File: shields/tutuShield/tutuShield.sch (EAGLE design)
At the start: 23 parts, among them IC1 IC_MSGEQ7-SOIC8, Q4 2N3904

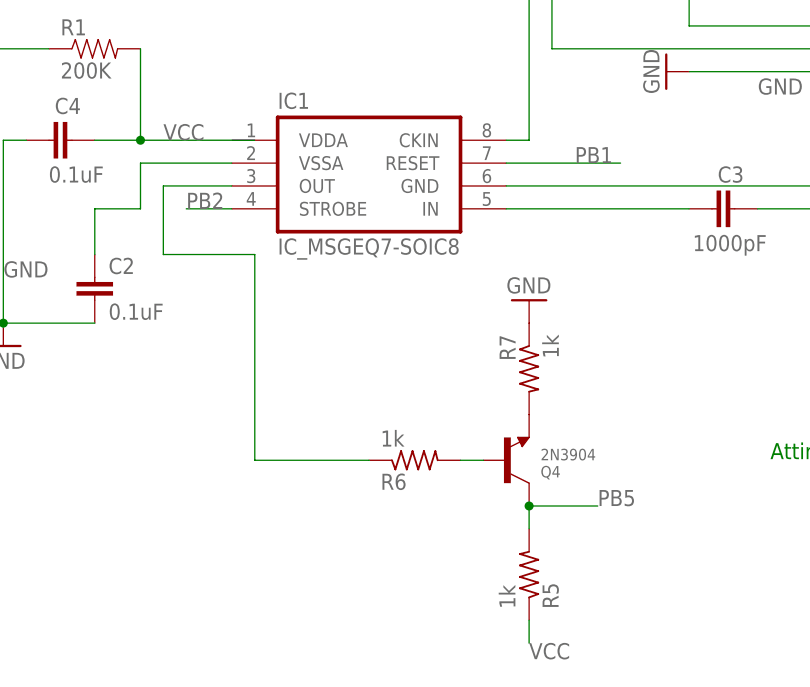
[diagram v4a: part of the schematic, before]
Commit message: a version without the PB5 trick
it might be a bit simpler but i think its worth it to stick to
4af68e7c457e82ac5364ccc3b228164f2045e11b
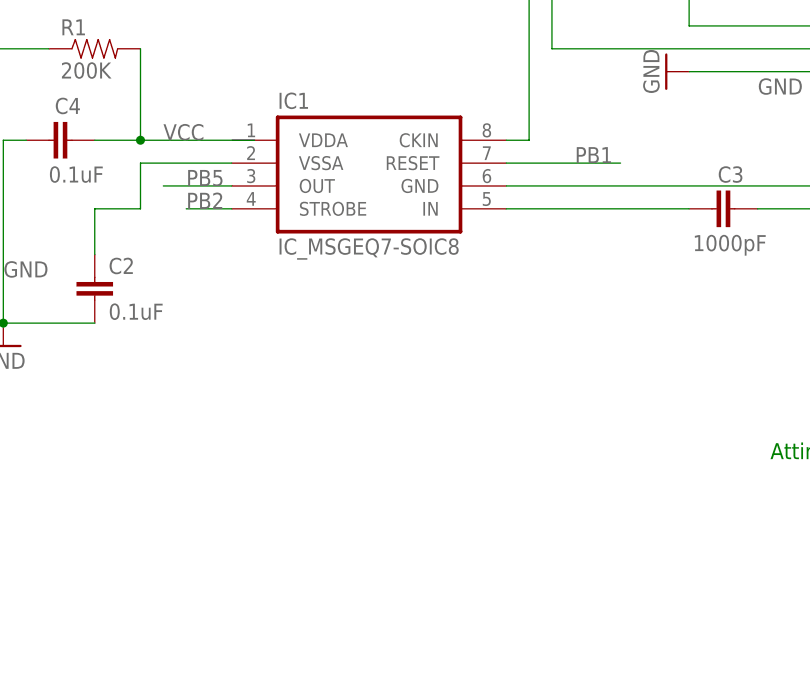
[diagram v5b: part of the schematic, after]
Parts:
- removed Q4: 2N3904, microbuilder:TRANSISTOR_NPNWAVE
- removed R5, R6, R7: 1k, adafruit:R-US_R0805
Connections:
- removed net N$14: Q4.B, R6.2
- removed net N$8: Q4.E, R7.2
- net GND: no longer R7.1
- net PB1: no longer IC1.OUT, R6.1
- net PB5: now also IC1.OUT; no longer Q4.C, R5.2
- net VCC: no longer R5.1
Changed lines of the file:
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@@
 <part name="JP2" library="ATtami" deviceset="HEADER-1X4" device="ROUND"/>
 <part name="GND3" library="SparkFun" deviceset="GND" device=""/>
-<part name="R5" library="adafruit" deviceset="R-US_" device="R0805" value="1k"/>
-<part name="Q4" library="microbuilder" deviceset="TRANSISTOR_NPN" device="WAVE" value="2N3904"/>
-<part name="R6" library="adafruit" deviceset="R-US_" device="R0805" value="1k"/>
-<part name="R7" library="adafruit" deviceset="R-US_" device="R0805" value="1k"/>
-<part name="GND4" library="SparkFun" deviceset="GND" device=""/>
 </parts>
 <sheets>
@@
 <instance part="JP2" gate="A" x="180.34" y="104.14"/>
 <instance part="GND3" gate="1" x="149.86" y="96.52" rot="R270"/>
-<instance part="R5" gate="G$1" x="134.62" y="40.64" rot="MR90"/>
-<instance part="Q4" gate="G$1" x="134.62" y="53.34" rot="MR180"/>
-<instance part="R6" gate="G$1" x="121.92" y="53.34" rot="MR180"/>
-<instance part="R7" gate="G$1" x="134.62" y="63.5" rot="MR270"/>
-<instance part="GND4" gate="1" x="134.62" y="71.12" rot="MR180"/>
 </instances>
 <busses>
@@
 <pinref part="GND3" gate="1" pin="GND"/>
 </segment>
-<segment>
-<pinref part="R7" gate="G$1" pin="1"/>
-<pinref part="GND4" gate="1" pin="GND"/>
-</segment>
 </net>
 <net name="VCC" class="0">
@@
 </segment>
 <segment>
-<pinref part="R5" gate="G$1" pin="1"/>
-<wire x1="134.62" y1="35.56" x2="134.62" y2="33.02" width="0.1524" layer="91"/>
-<label x="134.62" y="33.02" size="1.778" layer="95" rot="MR180"/>
-</segment>
-<segment>
 <pinref part="C3" gate="G$1" pin="2"/>
 <pinref part="JP1" gate="G$1" pin="2"/>
@@
 </segment>
 <segment>
-<pinref part="IC1" gate="IC" pin="OUT"/>
-<wire x1="101.6" y1="83.82" x2="93.98" y2="83.82" width="0.1524" layer="91"/>
-<wire x1="93.98" y1="83.82" x2="93.98" y2="76.2" width="0.1524" layer="91"/>
-<wire x1="93.98" y1="76.2" x2="104.14" y2="76.2" width="0.1524" layer="91"/>
-<wire x1="104.14" y1="76.2" x2="104.14" y2="53.34" width="0.1524" layer="91"/>
-<pinref part="R6" gate="G$1" pin="1"/>
-<wire x1="104.14" y1="53.34" x2="116.84" y2="53.34" width="0.1524" layer="91"/>
-</segment>
-<segment>
 <pinref part="IC1" gate="IC" pin="RESET"/>
 <wire x1="132.08" y1="86.36" x2="144.78" y2="86.36" width="0.1524" layer="91"/>
@@
 </segment>
 <segment>
-<pinref part="R5" gate="G$1" pin="2"/>
-<pinref part="Q4" gate="G$1" pin="C"/>
-<wire x1="134.62" y1="45.72" x2="134.62" y2="48.26" width="0.1524" layer="91"/>
-<wire x1="134.62" y1="48.26" x2="142.24" y2="48.26" width="0.1524" layer="91"/>
-<junction x="134.62" y="48.26"/>
-<label x="142.24" y="48.26" size="1.778" layer="95"/>
+<pinref part="IC1" gate="IC" pin="OUT"/>
+<wire x1="101.6" y1="83.82" x2="93.98" y2="83.82" width="0.1524" layer="91"/>
+<label x="96.52" y="83.82" size="1.778" layer="95"/>
 </segment>
 </net>
@@
 </segment>
 </net>
-<net name="N$8" class="0">
-<segment>
-<pinref part="R7" gate="G$1" pin="2"/>
-<pinref part="Q4" gate="G$1" pin="E"/>
-</segment>
-</net>
-<net name="N$14" class="0">
-<segment>
-<pinref part="Q4" gate="G$1" pin="B"/>
-<pinref part="R6" gate="G$1" pin="2"/>
-<wire x1="129.54" y1="53.34" x2="127" y2="53.34" width="0.1524" layer="91"/>
-</segment>
-</net>

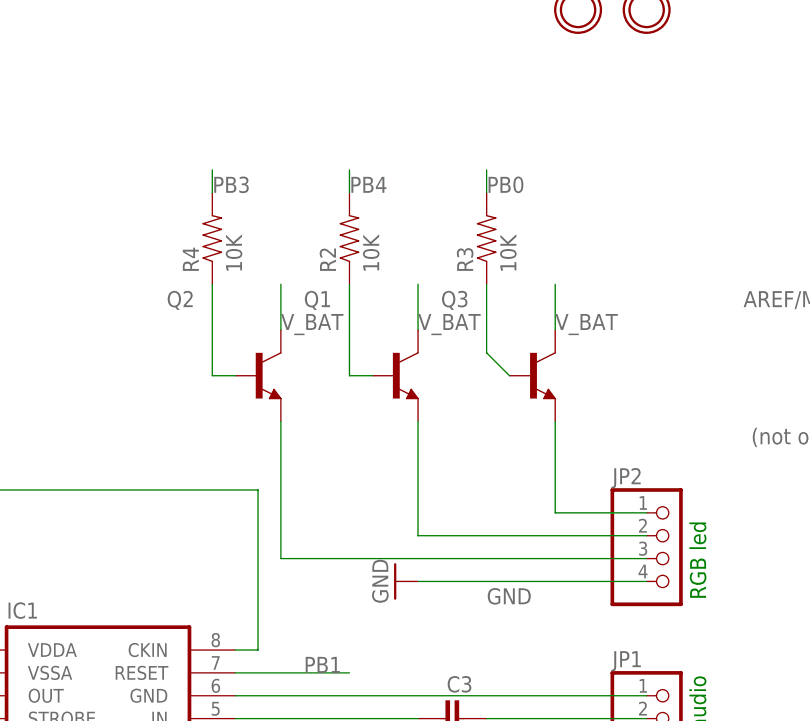
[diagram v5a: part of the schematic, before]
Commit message: routed
without the PB5
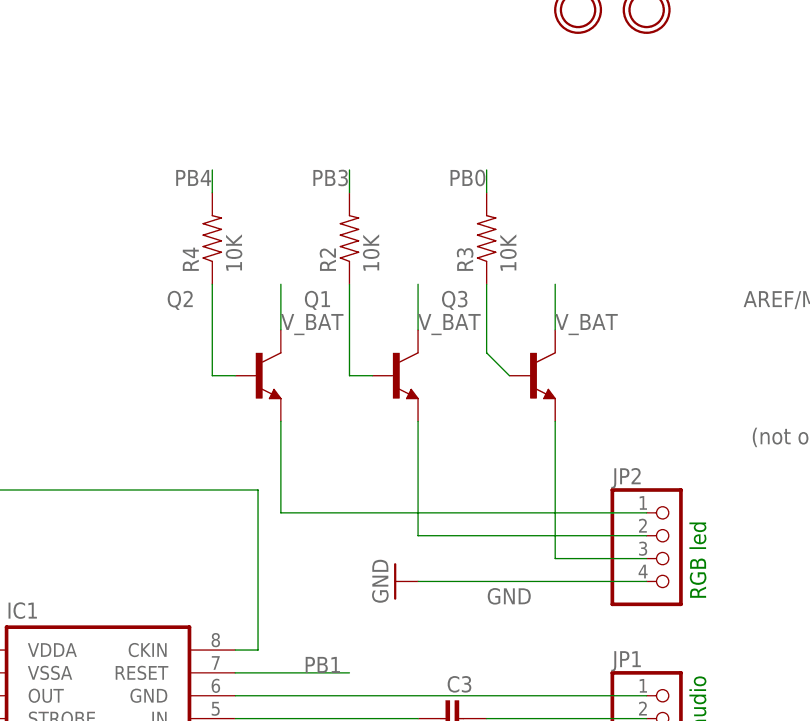
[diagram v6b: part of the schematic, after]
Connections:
- net N$10: now also JP2.1; no longer JP2.3
- net N$13: now also JP2.3; no longer JP2.1
- net PB3: now also R2.2; no longer R4.2
- net PB4: now also R4.2; no longer R2.2
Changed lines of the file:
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@@
 <pinref part="R3" gate="G$1" pin="2"/>
 <wire x1="160.02" y1="139.7" x2="160.02" y2="142.24" width="0.1524" layer="91"/>
-<label x="160.02" y="139.7" size="1.778" layer="95"/>
+<label x="160.02" y="142.24" size="1.778" layer="95" rot="R180"/>
 </segment>
 </net>
@@
 </segment>
 <segment>
-<pinref part="R4" gate="G$1" pin="2"/>
-<wire x1="129.54" y1="139.7" x2="129.54" y2="142.24" width="0.1524" layer="91"/>
-<label x="129.54" y="139.7" size="1.778" layer="95"/>
+<pinref part="R2" gate="G$1" pin="2"/>
+<wire x1="144.78" y1="139.7" x2="144.78" y2="142.24" width="0.1524" layer="91"/>
+<label x="144.78" y="142.24" size="1.778" layer="95" rot="R180"/>
 </segment>
 </net>
@@
 </segment>
 <segment>
-<pinref part="R2" gate="G$1" pin="2"/>
-<wire x1="144.78" y1="139.7" x2="144.78" y2="142.24" width="0.1524" layer="91"/>
-<label x="144.78" y="139.7" size="1.778" layer="95"/>
+<pinref part="R4" gate="G$1" pin="2"/>
+<wire x1="129.54" y1="139.7" x2="129.54" y2="142.24" width="0.1524" layer="91"/>
+<label x="129.54" y="142.24" size="1.778" layer="95" rot="R180"/>
 </segment>
 </net>
@@
 <segment>
 <pinref part="Q2" gate="Q" pin="E"/>
-<wire x1="137.16" y1="114.3" x2="137.16" y2="99.06" width="0.1524" layer="91"/>
-<pinref part="JP2" gate="A" pin="3"/>
-<wire x1="137.16" y1="99.06" x2="177.8" y2="99.06" width="0.1524" layer="91"/>
+<wire x1="137.16" y1="114.3" x2="137.16" y2="104.14" width="0.1524" layer="91"/>
+<pinref part="JP2" gate="A" pin="1"/>
+<wire x1="177.8" y1="104.14" x2="137.16" y2="104.14" width="0.1524" layer="91"/>
 </segment>
 </net>
@@
 <segment>
 <pinref part="Q3" gate="Q" pin="E"/>
-<wire x1="167.64" y1="114.3" x2="167.64" y2="104.14" width="0.1524" layer="91"/>
-<pinref part="JP2" gate="A" pin="1"/>
-<wire x1="167.64" y1="104.14" x2="177.8" y2="104.14" width="0.1524" layer="91"/>
+<wire x1="167.64" y1="114.3" x2="167.64" y2="99.06" width="0.1524" layer="91"/>
+<pinref part="JP2" gate="A" pin="3"/>
+<wire x1="167.64" y1="99.06" x2="177.8" y2="99.06" width="0.1524" layer="91"/>
 </segment>
 </net>

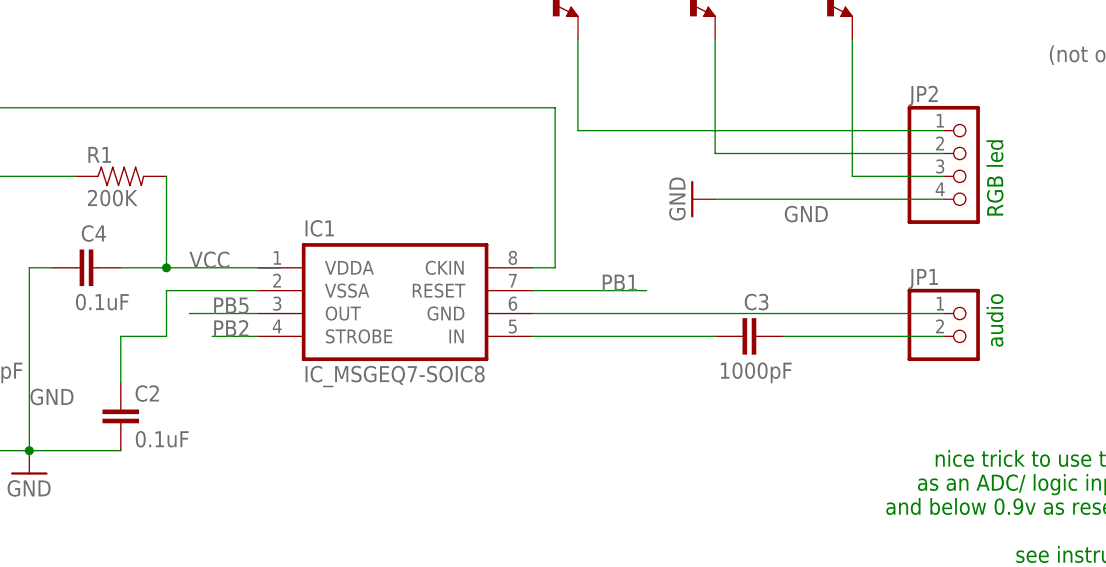
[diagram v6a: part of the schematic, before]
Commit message: fix GND and VCC airwires
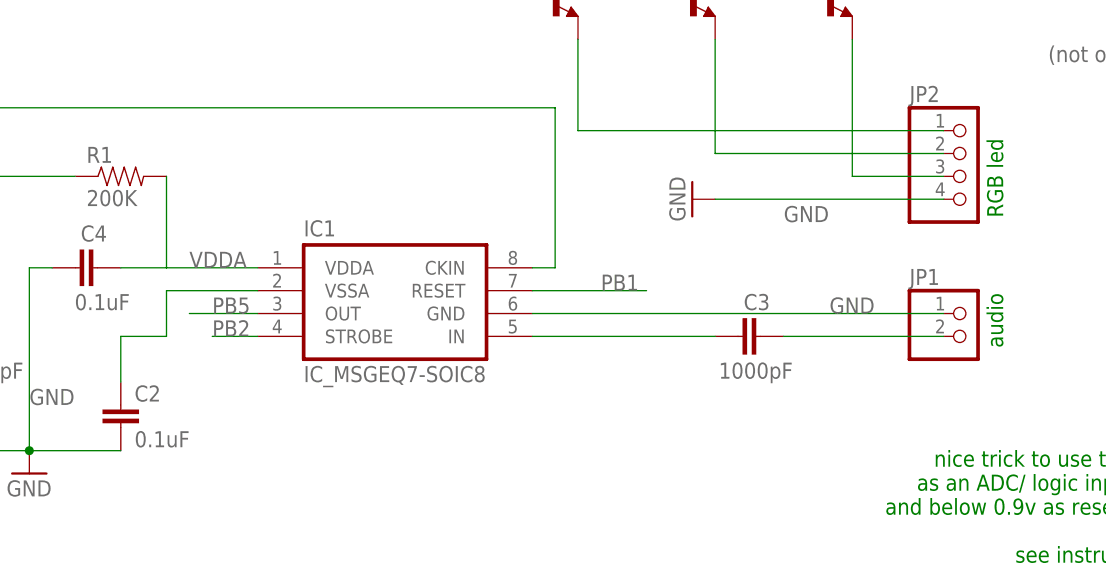
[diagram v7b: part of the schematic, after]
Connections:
- removed net N$4: IC1.GND, JP1.1
- new net VDDA: C4.2, IC1.VDDA, R1.2
- net GND: now also IC1.GND, JP1.1
- net VCC: no longer C4.2, R1.2
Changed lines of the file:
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@@
 <?xml version="1.0" encoding="utf-8"?>
 <!DOCTYPE eagle SYSTEM "eagle.dtd">
-<eagle version="7.1.0">
+<eagle version="7.2.0">
 <drawing>
 <settings>
@@
 <pinref part="GND3" gate="1" pin="GND"/>
 </segment>
+<segment>
+<pinref part="JP1" gate="G$1" pin="1"/>
+<pinref part="IC1" gate="IC" pin="GND"/>
+<wire x1="177.8" y1="83.82" x2="132.08" y2="83.82" width="0.1524" layer="91"/>
+<label x="165.1" y="83.82" size="1.778" layer="95"/>
+</segment>
 </net>
 <net name="VCC" class="0">
@@
 </segment>
 <segment>
-<pinref part="C4" gate="G$1" pin="2"/>
-<wire x1="104.14" y1="88.9" x2="91.44" y2="88.9" width="0.1524" layer="91"/>
-<label x="93.98" y="88.9" size="1.778" layer="95"/>
-<pinref part="R1" gate="G$1" pin="2"/>
-<wire x1="91.44" y1="88.9" x2="86.36" y2="88.9" width="0.1524" layer="91"/>
-<wire x1="91.44" y1="99.06" x2="91.44" y2="88.9" width="0.1524" layer="91"/>
-<junction x="91.44" y="88.9"/>
-</segment>
-<segment>
 <pinref part="C3" gate="G$1" pin="2"/>
 <pinref part="JP1" gate="G$1" pin="2"/>
@@
 <pinref part="C3" gate="G$1" pin="1"/>
 <wire x1="132.08" y1="81.28" x2="152.4" y2="81.28" width="0.1524" layer="91"/>
-</segment>
-</net>
-<net name="N$4" class="0">
-<segment>
-<pinref part="IC1" gate="IC" pin="GND"/>
-<pinref part="JP1" gate="G$1" pin="1"/>
-<wire x1="132.08" y1="83.82" x2="177.8" y2="83.82" width="0.1524" layer="91"/>
 </segment>
 </net>
@@
 </segment>
 </net>
+<net name="VDDA" class="0">
+<segment>
+<pinref part="C4" gate="G$1" pin="2"/>
+<label x="93.98" y="88.9" size="1.778" layer="95"/>
+<pinref part="R1" gate="G$1" pin="2"/>
+<wire x1="91.44" y1="88.9" x2="86.36" y2="88.9" width="0.1524" layer="91"/>
+<wire x1="91.44" y1="99.06" x2="91.44" y2="88.9" width="0.1524" layer="91"/>
+<pinref part="IC1" gate="IC" pin="VDDA"/>
+<wire x1="91.44" y1="88.9" x2="101.6" y2="88.9" width="0.1524" layer="91"/>
+</segment>
+</net>

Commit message: added tutu logo and BMP file
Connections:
- new net N$1: C3.2, JP1.2
- net VCC: no longer C3.2, JP1.2
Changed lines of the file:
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@@
 <label x="86.868" y="145.288" size="1.778" layer="95"/>
-</segment>
-<segment>
-<pinref part="C3" gate="G$1" pin="2"/>
-<pinref part="JP1" gate="G$1" pin="2"/>
-<wire x1="160.02" y1="81.28" x2="177.8" y2="81.28" width="0.1524" layer="91"/>
 </segment>
 </net>
@@
 </segment>
 </net>
+<net name="N$1" class="0">
+<segment>
+<pinref part="C3" gate="G$1" pin="2"/>
+<pinref part="JP1" gate="G$1" pin="2"/>
+<wire x1="160.02" y1="81.28" x2="177.8" y2="81.28" width="0.1524" layer="91"/>
+</segment>
+</net>
